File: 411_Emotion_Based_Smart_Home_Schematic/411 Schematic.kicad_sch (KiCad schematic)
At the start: 24 parts, among them Q1 NSS1C301ET4G, Q2 NSS1C301ET4G, Q3 NSS1C301ET4G, U4 HC-SR04

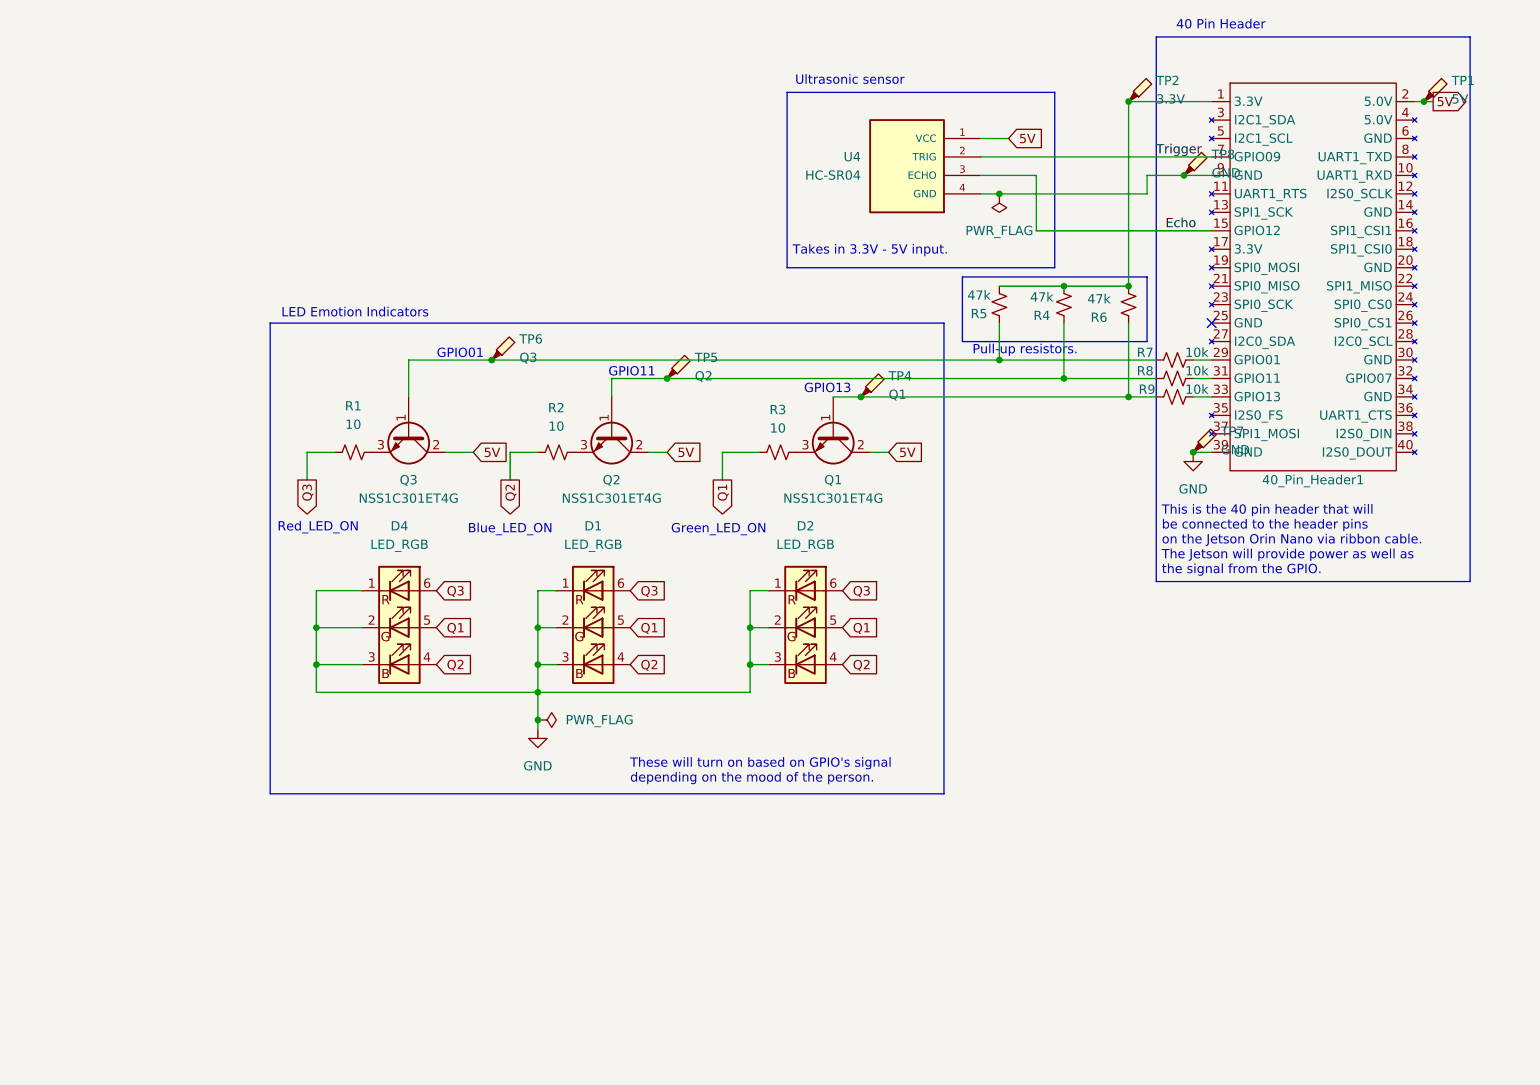
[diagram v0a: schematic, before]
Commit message: Updated schematic again. Should work now.
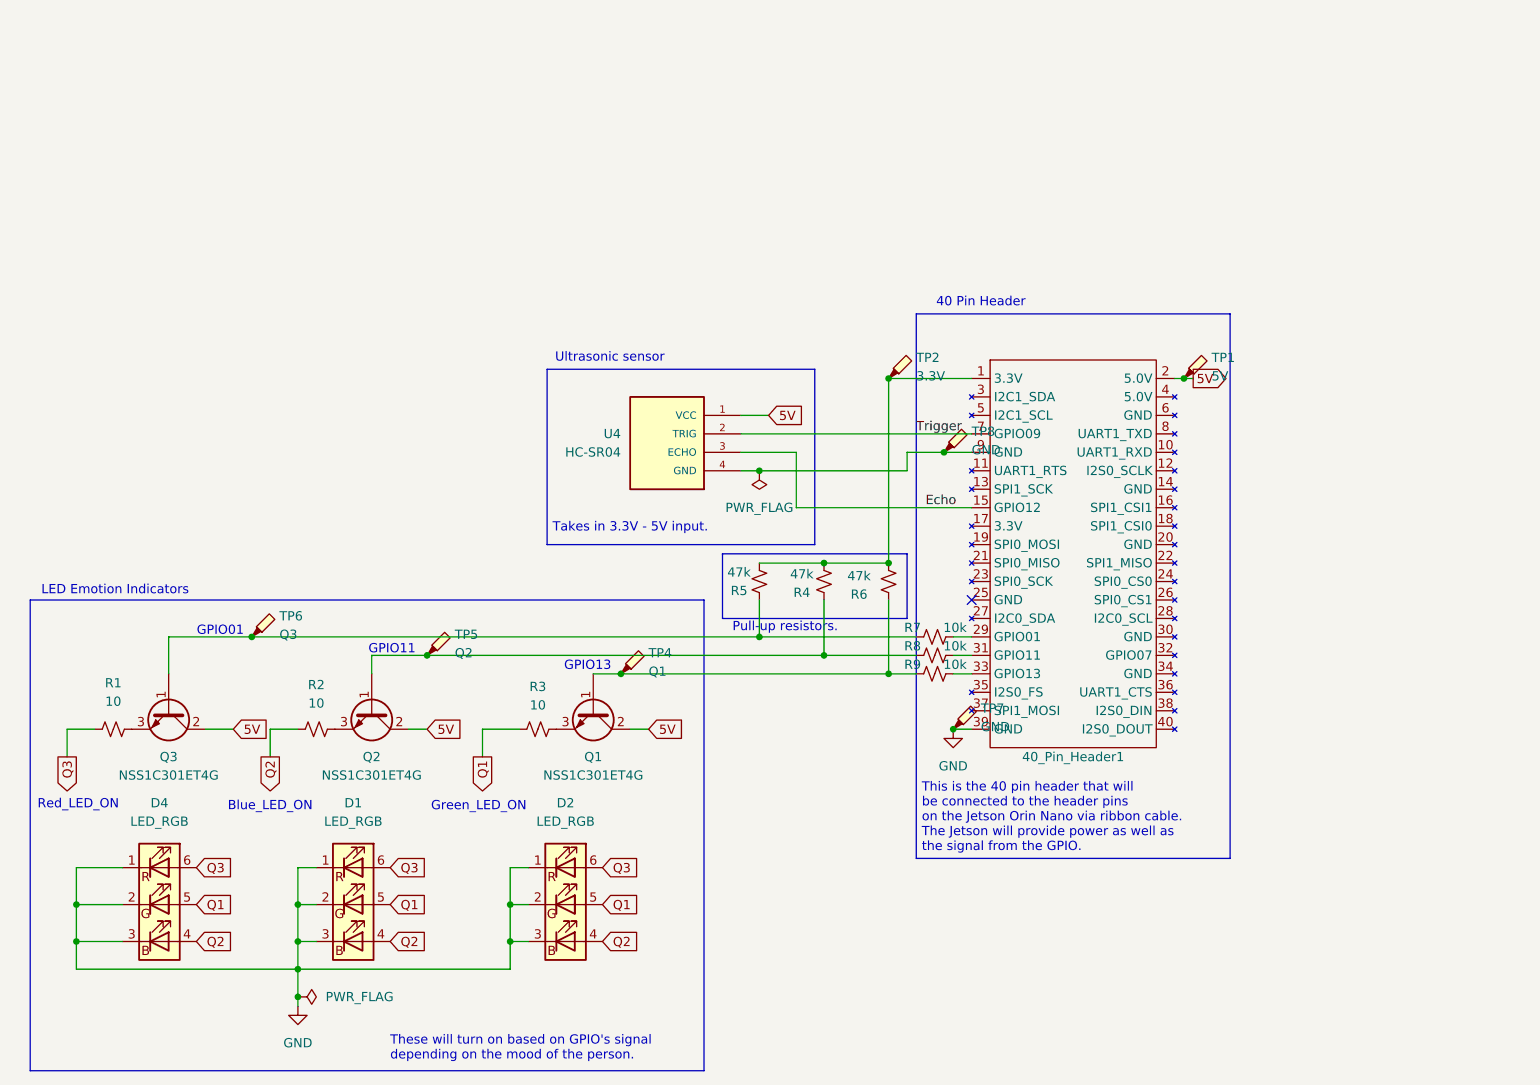
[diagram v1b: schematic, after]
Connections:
- net at 40_Pin_Header1.29 (GPIO01): now also R7.2; no longer R7.1
- net at 40_Pin_Header1.31 (GPIO11): now also R8.2; no longer R8.1
- net at 40_Pin_Header1.33 (GPIO13): now also R9.2; no longer R9.1
- net at Q3.1 (B), R5.2, TP6.1: now also R7.1; no longer R7.2
- net at Q2.1 (B), R4.2, TP5.1: now also R8.1; no longer R8.2
- net at Q1.1 (B), R6.2, TP4.1: now also R9.1; no longer R9.2
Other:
- moved on the sheet: 40_Pin_Header1, D1, D2, D4, Q1, Q2, Q3, R1, R2, R3, R4, R5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

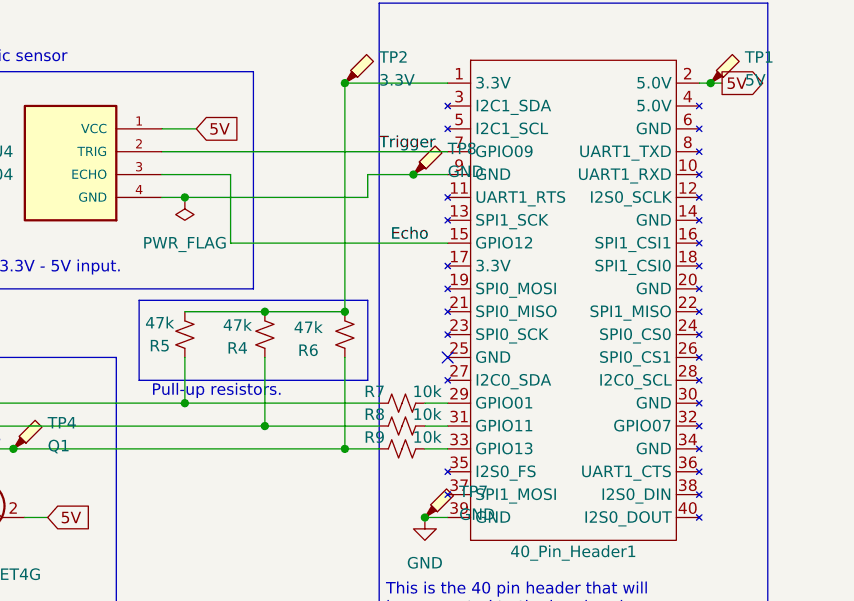
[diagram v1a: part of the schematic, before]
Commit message: Updated schematic.
Changed from Pin 15 to Pin 32.
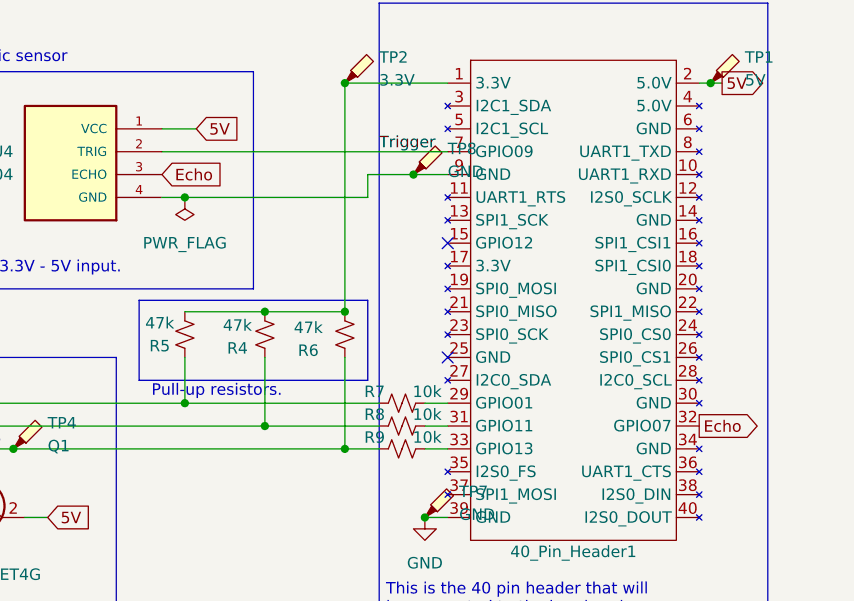
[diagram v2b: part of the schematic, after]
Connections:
- net Echo: now also 40_Pin_Header1.32 (GPIO07); no longer 40_Pin_Header1.15 (GPIO12)
- no-connect marks 1 -> 2
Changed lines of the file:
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@@
+	)
+	(no_connect
+		(at 165.1 102.87)
 	)
 	(no_connect
@@
 	(wire
 		(pts
-			(xy 140.97 95.25) (xy 140.97 102.87)
-		)
-		(stroke
-			(width 0)
-			(type default)
-		)
-	)
-	(wire
-		(pts
 			(xy 135.89 115.57) (xy 135.89 120.65)
 		)
@@
 	(wire
 		(pts
-			(xy 140.97 102.87) (xy 165.1 102.87)
-		)
-		(stroke
-			(width 0)
-			(type default)
-		)
-	)
-	(wire
-		(pts
 			(xy 162.56 123.19) (xy 165.1 123.19)
 		)
@@
 		(pts
 			(xy 156.21 95.25) (xy 161.29 95.25)
-		)
-		(stroke
-			(width 0)
-			(type default)
-		)
-	)
-	(wire
-		(pts
-			(xy 133.35 95.25) (xy 140.97 95.25)
 		)
 		(stroke
@@
 				(size 1.27 1.27)
 			)
-		)
-	)
-	(label "Echo"
-		(at 158.75 102.87 0)
-		(fields_autoplaced yes)
-		(effects
-			(font
-				(size 1.27 1.27)
-			)
-			(justify left bottom)
 		)
 	)
@@
 		)
 	)
+	(global_label "Echo"
+		(shape input)
+		(at 133.35 95.25 0)
+		(fields_autoplaced yes)
+		(effects
+			(font
+				(size 1.27 1.27)
+			)
+			(justify left)
+		)
+		(property "Intersheetrefs" "${INTERSHEET_REFS}"
+			(at 140.8708 95.25 0)
+			(effects
+				(font
+					(size 1.27 1.27)
+				)
+				(justify left)
+				(hide yes)
+			)
+		)
+	)
 	(global_label "Q1"
 		(shape input)
@@
 			(effects
 				(font
+					(size 1.27 1.27)
+				)
+				(justify left)
+				(hide yes)
+			)
+		)
+	)
+	(global_label "Echo"
+		(shape output)
+		(at 193.04 123.19 0)
+		(fields_autoplaced yes)
+		(effects
+			(font
+				(size 1.27 1.27)
+			)
+			(justify left)
+		)
+		(property "Intersheetrefs" "${INTERSHEET_REFS}"
+			(at 200.5608 123.19 0)
+			(effects
+				(font
